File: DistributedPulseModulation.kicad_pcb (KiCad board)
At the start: 2 copper layers, 95.9 x 90.2 mm, 52 parts, among them J1 Conn_02x12_Odd_Even, J2 Conn_01x01, U1 74LS251, U10 4053, U11 4053, U12 4053, U2 74LVC2G74, U25 74LS85, U28 74LS85, U31 74LS85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

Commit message: V2.0 : SCH + PCB + Gerber
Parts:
- removed kibuzzard-680E1DF3: G***, kibuzzard-680E1DF3
- removed kibuzzard-680E1DFA: G***, kibuzzard-680E1DFA
- removed kibuzzard-68101858: G***, kibuzzard-68101858
- removed kibuzzard-681018C7: G***, kibuzzard-681018C7
- added kibuzzard-6811091F: G***, kibuzzard-6811091F, F.Cu at (67.3, 116.8)
- added kibuzzard-68110930: G***, kibuzzard-68110930, F.Cu at (49.5, 116.8)
- added kibuzzard-68110D32: G***, kibuzzard-68110D32, F.Cu at (58.4, 120.0)
- moved kibuzzard-680E1E0B 5.99 mm to (78.7, 127.0)
- moved kibuzzard-680E1E1F 5.99 mm to (66.0, 127.0)
- moved JP5 2.84 mm to (61.0, 116.8), turned to -90 degrees
- moved J2 1.27 mm to (58.4, 123.2)
- turned ByPass_2G74 to 180 degrees
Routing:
- net +5V: track 534.2 -> 523.2 mm
- net /Clock_loc: track 70.6 -> 81.5 mm
- net DPM_PWM: track 125.5 -> 130.9 mm
- net VBatt: track 53.0 -> 56.8 mm
- net DPM: track 21.4 -> 24.9 mm
- net ~{Reset}: track 54.8 -> 57.7 mm
- net Ground: track 860.3 -> 857.8 mm
- net Net-(ByPass_2G74-A): track 13.9 -> 11.5 mm
- net DDPM: track 102.4 -> 100.7 mm
- net /Div_2: track 26.5 -> 25.1 mm
- net SDA: track 41.9 -> 41.1 mm

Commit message: PCB_V2.0 delivery and README.md update
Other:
- board text removed: "Out"
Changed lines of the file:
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@@
 		(sheetname "/")
 		(sheetfile "DistributedPulseModulation.kicad_sch")
-		(attr through_hole)
+		(attr through_hole exclude_from_pos_files exclude_from_bom dnp)
 		(fp_line
 			(start 6.46 19.11)
@@
 		(sheetname "/")
 		(sheetfile "DistributedPulseModulation.kicad_sch")
-		(attr through_hole)
+		(attr through_hole exclude_from_pos_files exclude_from_bom dnp)
 		(fp_line
 			(start -0.12 1.37)
@@
 		(sheetname "/")
 		(sheetfile "DistributedPulseModulation.kicad_sch")
-		(attr through_hole)
+		(attr through_hole exclude_from_pos_files exclude_from_bom dnp)
 		(fp_line
 			(start 5.12 -1.37)
@@
 		(sheetname "/")
 		(sheetfile "DistributedPulseModulation.kicad_sch")
-		(attr through_hole)
+		(attr through_hole exclude_from_pos_files exclude_from_bom dnp)
 		(fp_line
 			(start 6.46 19.11)
@@
 		(sheetname "/")
 		(sheetfile "DistributedPulseModulation.kicad_sch")
-		(attr through_hole)
+		(attr through_hole exclude_from_pos_files exclude_from_bom dnp)
 		(fp_line
 			(start 6.46 19.11)
@@
 		(sheetname "/")
 		(sheetfile "DistributedPulseModulation.kicad_sch")
-		(attr through_hole)
+		(attr through_hole exclude_from_pos_files exclude_from_bom dnp)
 		(fp_line
 			(start 5.12 -1.37)
@@
 		)
 	)
-	(gr_text "Out"
-		(at 50.8 130.175 0)
-		(layer "F.SilkS")
-		(effects
-			(font
-				(size 2 2)
-				(thickness 0.5)
-				(bold yes)
-			)
-			(justify left)
-		)
-	)

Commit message: Routage : légère modif de la route du GND
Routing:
- net Ground: track 857.8 -> 891.8 mm
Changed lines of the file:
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@@
+	)
+	(segment
+		(start 71.12 127)
+		(end 71.12 125.095)
+		(width 1)
+		(layer "F.Cu")
+		(net 11)
 	)
 	(segment
@@
 	)
 	(segment
+		(start 83.4025 122.9725)
+		(end 83.4025 120.015)
+		(width 1)
+		(layer "F.Cu")
+		(net 11)
+	)
+	(segment
 		(start 72.39 130.175)
 		(end 71.12 128.905)
@@
 		(end 83.185 51.435)
 		(width 0.5)
+		(layer "F.Cu")
+		(net 11)
+	)
+	(segment
+		(start 72.39 123.825)
+		(end 82.55 123.825)
+		(width 1)
 		(layer "F.Cu")
 		(net 11)
@@
 	)
 	(segment
+		(start 82.55 123.825)
+		(end 83.4025 122.9725)
+		(width 1)
+		(layer "F.Cu")
+		(net 11)
+	)
+	(segment
 		(start 46.355 104.14)
 		(end 44.45 104.14)
@@
 		(end 50.165 48.26)
 		(width 0.5)
+		(layer "F.Cu")
+		(net 11)
+	)
+	(segment
+		(start 71.12 125.095)
+		(end 72.39 123.825)
+		(width 1)
 		(layer "F.Cu")
 		(net 11)
@@
 	)
 	(segment
+		(start 99.06 118.11)
+		(end 99.06 121.92)
+		(width 0.5)
+		(layer "B.Cu")
+		(net 11)
+	)
+	(segment
 		(start 106.68 119.38)
 		(end 107.95 120.65)
@@
 		(start 132.08 58.34)
 		(end 132.08 49.53)
+		(width 0.5)
+		(layer "B.Cu")
+		(net 11)
+	)
+	(segment
+		(start 99.06 121.92)
+		(end 99.14 121.92)
 		(width 0.5)
 		(layer "B.Cu")
@@
 	)
 	(segment
+		(start 104.775 117.475)
+		(end 99.695 117.475)
+		(width 0.5)
+		(layer "B.Cu")
+		(net 11)
+	)
+	(segment
 		(start 107.95 120.65)
 		(end 109.22 119.38)
@@
 	)
 	(segment
+		(start 106.68 119.38)
+		(end 104.775 117.475)
+		(width 0.5)
+		(layer "B.Cu")
+		(net 11)
+	)
+	(segment
 		(start 110.49 120.65)
 		(end 111.76 119.38)
@@
 		(start 113.03 61.595)
 		(end 113.03 52.07)
+		(width 0.5)
+		(layer "B.Cu")
+		(net 11)
+	)
+	(segment
+		(start 99.695 117.475)
+		(end 99.06 118.11)
 		(width 0.5)
 		(layer "B.Cu")
@@
 		(width 0.5)
 		(layer "B.Cu")
+		(net 11)
+	)
+	(segment
+		(start 99.14 121.92)
+		(end 101.6 124.38)
+		(width 0.5)
+		(layer "B.Cu")

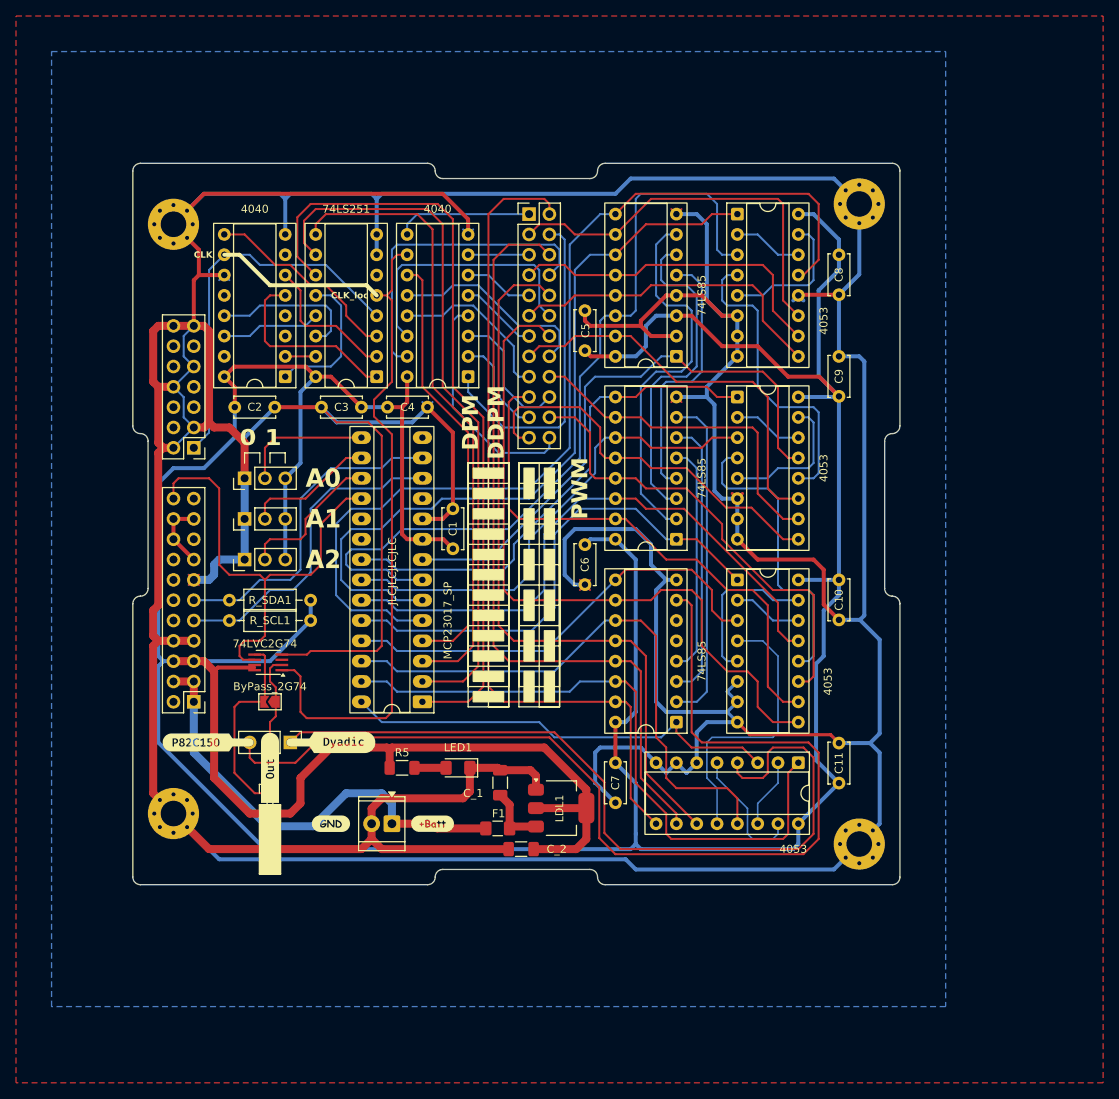
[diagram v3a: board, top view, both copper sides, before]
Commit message: Ajout test-points pour les ports A et B du MCP23017 Léger reroutage
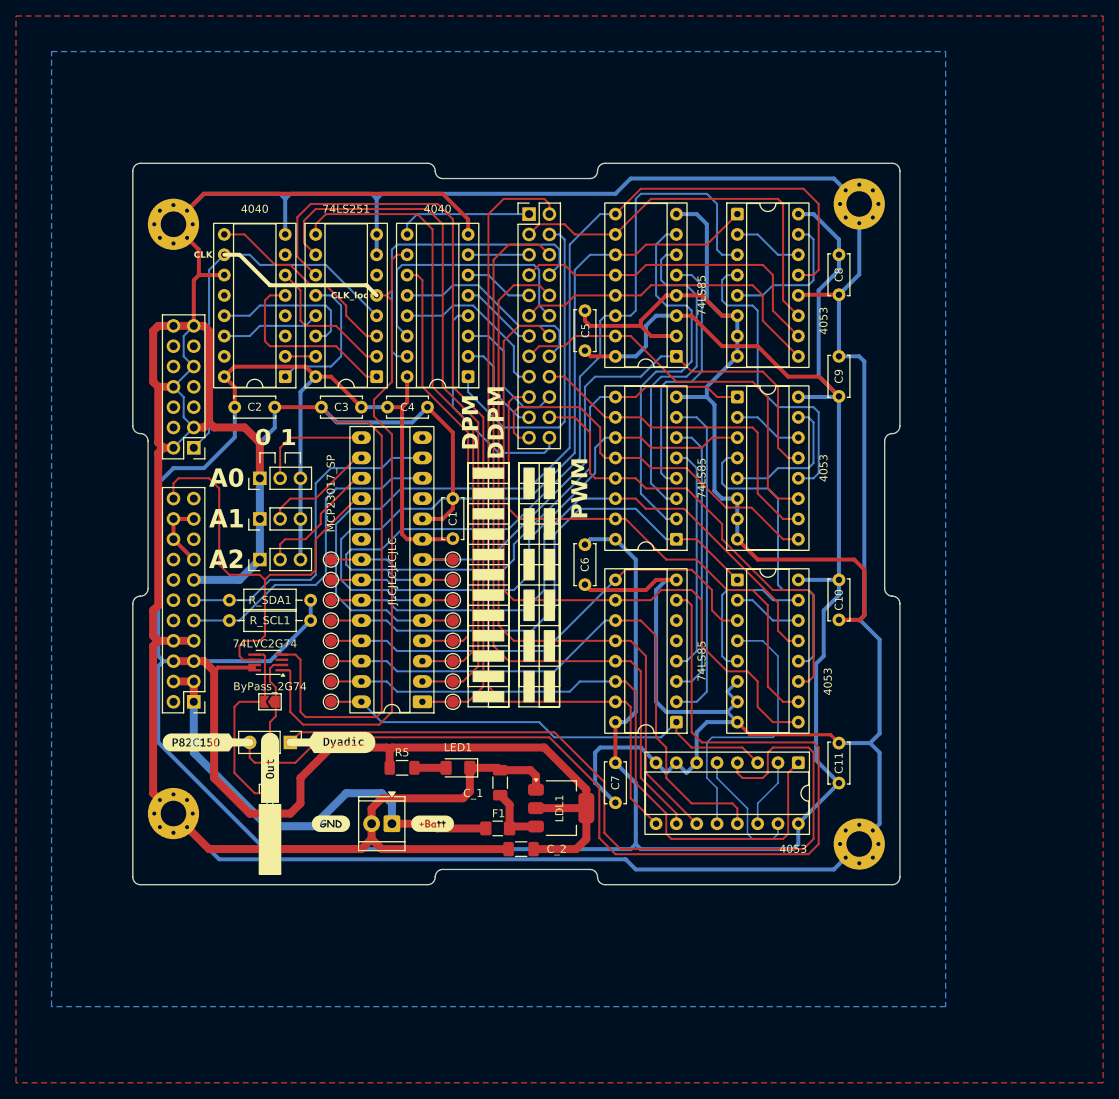
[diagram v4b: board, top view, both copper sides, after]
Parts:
- added TP_A0: TestPoint_Probe, TestPoint:TestPoint_Pad_D1.5mm, F.Cu at (81.3, 101.6)
- added TP_A1: TestPoint_Probe, TestPoint:TestPoint_Pad_D1.5mm, F.Cu at (81.3, 99.1)
- added TP_A10: TestPoint_Probe, TestPoint:TestPoint_Pad_D1.5mm, F.Cu at (66.0, 109.2)
- added TP_A11: TestPoint_Probe, TestPoint:TestPoint_Pad_D1.5mm, F.Cu at (66.0, 111.8)
- added TP_A2: TestPoint_Probe, TestPoint:TestPoint_Pad_D1.5mm, F.Cu at (81.3, 96.5)
- added TP_A3: TestPoint_Probe, TestPoint:TestPoint_Pad_D1.5mm, F.Cu at (81.3, 94.0)
- added TP_A4: TestPoint_Probe, TestPoint:TestPoint_Pad_D1.5mm, F.Cu at (66.0, 94.0)
- added TP_A5: TestPoint_Probe, TestPoint:TestPoint_Pad_D1.5mm, F.Cu at (66.0, 96.5)
- added TP_A6: TestPoint_Probe, TestPoint:TestPoint_Pad_D1.5mm, F.Cu at (66.0, 99.1)
- added TP_A7: TestPoint_Probe, TestPoint:TestPoint_Pad_D1.5mm, F.Cu at (66.0, 101.6)
- added TP_A8: TestPoint_Probe, TestPoint:TestPoint_Pad_D1.5mm, F.Cu at (66.0, 104.1)
- added TP_A9: TestPoint_Probe, TestPoint:TestPoint_Pad_D1.5mm, F.Cu at (66.0, 106.7)
- added TP_PS0: TestPoint_Probe, TestPoint:TestPoint_Pad_D1.5mm, F.Cu at (81.3, 111.8)
- added TP_PS1: TestPoint_Probe, TestPoint:TestPoint_Pad_D1.5mm, F.Cu at (81.3, 109.2)
- added TP_PS2: TestPoint_Probe, TestPoint:TestPoint_Pad_D1.5mm, F.Cu at (81.3, 106.7)
- added TP_~{CntEN}0: TestPoint_Probe, TestPoint:TestPoint_Pad_D1.5mm, F.Cu at (81.3, 104.1)
- moved JP1 1.91 mm to (57.1, 94.0)
- moved JP2 1.91 mm to (57.1, 88.9)
- moved JP3 1.91 mm to (57.1, 83.8)
- moved C1 1.27 mm to (81.3, 86.4)
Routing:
- net Ground: track 891.8 -> 881.5 mm
- net /A0: track 124.1 -> 129.2 mm
- net /A4: track 63.1 -> 66.9 mm
- net /A3: track 72.8 -> 76.6 mm
- net /A2: track 102.4 -> 106.2 mm
- net /A1: track 96.0 -> 99.9 mm
- net /A8: track 55.8 -> 59.7 mm
- net /A7: track 62.9 -> 66.7 mm
- net /A6: track 74.4 -> 78.2 mm
- net /A5: track 60.9 -> 64.7 mm
- net /A11: track 55.0 -> 58.8 mm
- net /A10: track 80.4 -> 84.2 mm
- net /A9: track 72.2 -> 75.3 mm
- net Net-(JP2-C): track 16.3 -> 14.1 mm
- net Net-(JP1-C): track 18.5 -> 16.2 mm
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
